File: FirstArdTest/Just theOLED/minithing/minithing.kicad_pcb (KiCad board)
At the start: 2 copper layers, 81.8 x 40.2 mm, 41 parts, among them IC1 DS3231MZ+, J1 USB4110-GF-A, Q1 NMOS, Q2 NMOS, Q3 FDN340P, SW1 SW_Push, SW2 SW_Push, SW3 SW_Push, SW4 SW_Push, U1 TP4056, U2 MT3608, U3 AHT20, U4 MCP23008-xSO

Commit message: Actual finish arduino pin change
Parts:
- SW3: footprint Button_Switch_THT:SW_PUSH_6mm_H4.3mm -> Button_Switch_THT:SW_PUSH_6mm
- U1: value TP4056 -> TP4056-42-ESOP8
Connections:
- A1 pad 19: unconnected-(A1-A0-Pad19) -> Net-(A1-A0)
- A1 pad 7: Net-(A1-D4) -> unconnected-(A1-D4-Pad7)
- C6 pad 2: Net-(A1-D4) -> Net-(A1-A0)
- R11 pad 1: Net-(A1-D4) -> Net-(A1-A0)
- R12 pad 1: Net-(A1-D4) -> Net-(A1-A0)
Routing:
- net Net-(A1-D4): track 52.5 -> 0.00 mm, vias 1 -> 0
- net (no net): track 0.00 -> 52.5 mm, vias 0 -> 1
- net Net-(A1-A0): track 0.00 -> 31.4 mm, vias 0 -> 1
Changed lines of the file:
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@@
 			(drillshape 0)
 			(scaleselection 1)
-			(outputdirectory "../")
+			(outputdirectory "../gbr files/")
 		)
 	)
@@
 	(net 13 "unconnected-(A1-D13-Pad16)")
 	(net 14 "5V out")
-	(net 15 "unconnected-(A1-A0-Pad19)")
+	(net 15 "Net-(A1-A0)")
 	(net 16 "unconnected-(A1-A3-Pad22)")
 	(net 17 "unconnected-(A1-~{RESET}-Pad28)")
@@
 	(net 25 "unconnected-(A1-D1{slash}TX-Pad1)")
 	(net 26 "unconnected-(A1-D8-Pad11)")
-	(net 27 "Net-(A1-D4)")
+	(net 27 "unconnected-(A1-D4-Pad7)")
 	(net 28 "1AMP")
 	(net 29 "Net-(D3-A)")
@@
 			(at 0 1.68 90)
 			(layer "F.Fab")
+			(hide yes)
 			(effects
 				(font
@@
 			(layers "F.Cu" "F.Mask" "F.Paste")
 			(roundrect_rratio 0.212766)
-			(net 27 "Net-(A1-D4)")
+			(net 15 "Net-(A1-A0)")
 			(pintype "passive")
 		)
@@
 			)
 		)
-		(property "Value" "TP4056"
+		(property "Value" "TP4056-42-ESOP8"
 			(at 0 3.4 0)
 			(layer "F.Fab")
@@
 			(layers "*.Cu" "*.Mask")
 			(remove_unused_layers no)
-			(net 27 "Net-(A1-D4)")
+			(net 27 "unconnected-(A1-D4-Pad7)")
 			(pinfunction "D4")
 			(pintype "bidirectional")
@@
 			(layers "*.Cu" "*.Mask")
 			(remove_unused_layers no)
-			(net 15 "unconnected-(A1-A0-Pad19)")
+			(net 15 "Net-(A1-A0)")
 			(pinfunction "A0")
 			(pintype "bidirectional")
@@
 			(layers "F.Cu" "F.Mask" "F.Paste")
 			(roundrect_rratio 0.208333)
-			(net 27 "Net-(A1-D4)")
+			(net 15 "Net-(A1-A0)")
 			(pintype "passive")
 		)
@@
 			(layers "F.Cu" "F.Mask" "F.Paste")
 			(roundrect_rratio 0.208333)
-			(net 27 "Net-(A1-D4)")
+			(net 15 "Net-(A1-A0)")
 			(pintype "passive")
 		)
@@
 		)
 	)
-	(footprint "Button_Switch_THT:SW_PUSH_6mm_H4.3mm"
+	(footprint "Button_Switch_THT:SW_PUSH_6mm"
 		(layer "F.Cu")
 		(at 47.3 63.5 90)
-		(descr "tactile push button, 6x6mm e.g. PHAP33xx series, height=4.3mm")
+		(descr "Generic 6mm SW tactile push button")
 		(tags "tact sw push 6mm")
 		(property "Reference" "SW3"
@@
 		)
 		(embedded_fonts no)
-		(model "${KICAD9_3DMODEL_DIR}/Button_Switch_THT.3dshapes/SW_PUSH_6mm_H4.3mm.step"
+		(model "${KICAD9_3DMODEL_DIR}/Button_Switch_THT.3dshapes/SW_PUSH_6mm.step"
 			(offset
 				(xyz 0 0 0)
@@
 	)
 	(segment
+		(start 71.75 35)
+		(end 71.75 36.75)
+		(width 0.2)
+		(layer "F.Cu")
+		(net 0)
+	)
+	(segment
+		(start 71.6 38.4)
+		(end 71.4 38.4)
+		(width 0.2)
+		(layer "F.Cu")
+		(net 0)
+	)
+	(segment
+		(start 71.75 36.75)
+		(end 71.75 38.25)
+		(width 0.2)
+		(layer "F.Cu")
+		(net 0)
+	)
+	(segment
+		(start 71.75 38.25)
+		(end 71.6 38.4)
+		(width 0.2)
+		(layer "F.Cu")
+		(net 0)
+	)
+	(segment
+		(start 71.4 38.4)
+		(end 71.3625 38.3625)
+		(width 0.2)
+		(layer "F.Cu")
+		(net 0)
+	)
+	(segment
+		(start 71.3625 38.3625)
+		(end 69.2 38.3625)
+		(width 0.2)
+		(layer "F.Cu")
+		(net 0)
+	)
+	(via
+		(at 71.75 36.75)
+		(size 0.6)
+		(drill 0.3)
+		(layers "F.Cu" "B.Cu")
+		(net 0)
+	)
+	(segment
+		(start 90.25 44)
+		(end 88.351 45.899)
+		(width 0.2)
+		(layer "B.Cu")
+		(net 0)
+	)
+	(segment
+		(start 76.75 41.75)
+		(end 89.75 41.75)
+		(width 0.2)
+		(layer "B.Cu")
+		(net 0)
+	)
+	(segment
+		(start 87.5 51)
+		(end 84 51)
+		(width 0.2)
+		(layer "B.Cu")
+		(net 0)
+	)
+	(segment
+		(start 88.351 45.899)
+		(end 88.351 50.149)
+		(width 0.2)
+		(layer "B.Cu")
+		(net 0)
+	)
+	(segment
+		(start 82 53)
+		(end 82 59)
+		(width 0.2)
+		(layer "B.Cu")
+		(net 0)
+	)
+	(segment
+		(start 82 59.25)
+		(end 82 59)
+		(width 0.2)
+		(layer "B.Cu")
+		(net 0)
+	)
+	(segment
+		(start 81.99 59.01)
+		(end 81.99 62.41)
+		(width 0.2)
+		(layer "B.Cu")
+		(net 0)
+	)
+	(segment
+		(start 84 51)
+		(end 82 53)
+		(width 0.2)
+		(layer "B.Cu")
+		(net 0)
+	)
+	(segment
+		(start 90.25 42.25)
+		(end 90.25 44)
+		(width 0.2)
+		(layer "B.Cu")
+		(net 0)
+	)
+	(segment
+		(start 89.75 41.75)
+		(end 90.25 42.25)
+		(width 0.2)
+		(layer "B.Cu")
+		(net 0)
+	)
+	(segment
+		(start 82 59)
+		(end 81.99 59.01)
+		(width 0.2)
+		(layer "B.Cu")
+		(net 0)
+	)
+	(segment
+		(start 88.351 50.149)
+		(end 87.5 51)
+		(width 0.2)
+		(layer "B.Cu")
+		(net 0)
+	)
+	(segment
+		(start 71.75 36.75)
+		(end 76.75 41.75)
+		(width 0.2)
+		(layer "B.Cu")
+		(net 0)
+	)
+	(segment
 		(start 57.9675 43.425001)
 		(end 57.492499 42.95)
@@
 	)
 	(segment
+		(start 70.46 36.72)
+		(end 69.3685 37.8115)
+		(width 0.5)
+		(layer "F.Cu")
+		(net 15)
+	)
+	(via
+		(at 70.46 36.72)
+		(size 0.6)
+		(drill 0.3)
+		(layers "F.Cu" "B.Cu")
+		(free yes)
+		(net 15)
+	)
+	(segment
+		(start 94.69 45.910768)
+		(end 84.778232 35.999)
+		(width 0.5)
+		(layer "B.Cu")
+		(net 15)
+	)
+	(segment
+		(start 94.69 47.17)
+		(end 94.69 45.910768)
+		(width 0.5)
+		(layer "B.Cu")
+		(net 15)
+	)
+	(segment
+		(start 84.778232 35.999)
+		(end 71.181 35.999)
+		(width 0.5)
+		(layer "B.Cu")
+		(net 15)
+	)
+	(segment
+		(start 71.181 35.999)
+		(end 70.46 36.72)
+		(width 0.5)
+		(layer "B.Cu")
+		(net 15)
+	)
+	(segment
 		(start 100.44 42.94)
 		(end 101 43.5)
@@
 	)
 	(segment
-		(start 71.75 35)
-		(end 71.75 36.75)
-		(width 0.2)
-		(layer "F.Cu")
-		(net 27)
-	)
-	(segment
-		(start 71.6 38.4)
-		(end 71.4 38.4)
-		(width 0.2)
-		(layer "F.Cu")
-		(net 27)
-	)
-	(segment
-		(start 71.75 36.75)
-		(end 71.75 38.25)
-		(width 0.2)
-		(layer "F.Cu")
-		(net 27)
-	)
-	(segment
-		(start 71.75 38.25)
-		(end 71.6 38.4)
-		(width 0.2)
-		(layer "F.Cu")
-		(net 27)
-	)
-	(segment
-		(start 71.4 38.4)
-		(end 71.3625 38.3625)
-		(width 0.2)
-		(layer "F.Cu")
-		(net 27)
-	)
-	(segment
-		(start 71.3625 38.3625)
-		(end 69.2 38.3625)
-		(width 0.2)
-		(layer "F.Cu")
-		(net 27)
-	)
-	(via
-		(at 71.75 36.75)
-		(size 0.6)
-		(drill 0.3)
-		(layers "F.Cu" "B.Cu")
-		(net 27)
-	)
-	(segment
-		(start 90.25 44)
-		(end 88.351 45.899)
-		(width 0.2)
-		(layer "B.Cu")
-		(net 27)
-	)
-	(segment
-		(start 76.75 41.75)
-		(end 89.75 41.75)
-		(width 0.2)
-		(layer "B.Cu")
-		(net 27)
-	)
-	(segment
-		(start 87.5 51)
-		(end 84 51)
-		(width 0.2)
-		(layer "B.Cu")
-		(net 27)
-	)
-	(segment
-		(start 88.351 45.899)
-		(end 88.351 50.149)
-		(width 0.2)
-		(layer "B.Cu")
-		(net 27)
-	)
-	(segment
-		(start 82 53)
-		(end 82 59)
-		(width 0.2)
-		(layer "B.Cu")
-		(net 27)
-	)
-	(segment
-		(start 82 59.25)
-		(end 82 59)
-		(width 0.2)
-		(layer "B.Cu")
-		(net 27)
-	)
-	(segment
-		(start 81.99 59.01)
-		(end 81.99 62.41)
-		(width 0.2)
-		(layer "B.Cu")
-		(net 27)
-	)
-	(segment
-		(start 84 51)
-		(end 82 53)
-		(width 0.2)
-		(layer "B.Cu")
-		(net 27)
-	)
-	(segment
-		(start 90.25 42.25)
-		(end 90.25 44)
-		(width 0.2)
-		(layer "B.Cu")
-		(net 27)
-	)
-	(segment
-		(start 89.75 41.75)
-		(end 90.25 42.25)
-		(width 0.2)
-		(layer "B.Cu")
-		(net 27)
-	)
-	(segment
-		(start 82 59)
-		(end 81.99 59.01)
-		(width 0.2)
-		(layer "B.Cu")
-		(net 27)
-	)
-	(segment
-		(start 88.351 50.149)
-		(end 87.5 51)
-		(width 0.2)
-		(layer "B.Cu")
-		(net 27)
-	)
-	(segment
-		(start 71.75 36.75)
-		(end 76.75 41.75)
-		(width 0.2)
-		(layer "B.Cu")
-		(net 27)
-	)
-	(segment

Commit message: Routine PCB ordered push, partial code
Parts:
- removed Z1: 1N4733A, SamacSys_Parts:DIOAD1405W86L465D235
- D2: footprint Diode_SMD:D_SMC_Handsoldering -> Diode_SMD:D_SMA
- moved C4 29.0 mm to (74.7, 27.4)
- moved D2 1.77 mm to (38.3, 34.3), turned to -90 degrees
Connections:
- A1 pad 27: 5V out -> 1AMP
- C4 pad 1: 1AMP -> Net-(Q3-D)
- C7 pad 1: 5V out -> 1AMP
- C8 pad 2: 5V out -> 1AMP
- D2 pad 1: GND -> 1AMP
- D2 pad 2: 1AMP -> GND
- D3 pad 1: 5V out -> 1AMP
- L1 pad 1: 1AMP -> Net-(Q3-D)
- Q3 pad 3: 1AMP -> Net-(Q3-D)
- R5 pad 2: 5V out -> 1AMP
- U2 pad 4: 1AMP -> Net-(Q3-D)
- U2 pad 5: 1AMP -> Net-(Q3-D)
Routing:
- net (no net): track 52.5 -> 0.00 mm, vias 1 -> 0
- net 1AMP: track 65.2 -> 87.5 mm, vias 2 -> 5
- net 5V out: track 19.3 -> 0.00 mm
- net Net-(Q3-D): track 0.00 -> 10.1 mm
- net Net-(A1-A0): track 31.4 -> 36.6 mm

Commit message: LastFinalFinalPush
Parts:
- added R13: 5.1KR, Resistor_SMD:R_0805_2012Metric_Pad1.20x1.40mm_HandSolder, F.Cu at (40.8, 50.3)
- added R14: 5.1KR, Resistor_SMD:R_0805_2012Metric_Pad1.20x1.40mm_HandSolder, F.Cu at (43.7, 50.3)
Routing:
- net Net-(A1-A4): track 55.6 -> 74.4 mm
- net Net-(A1-A5): track 60.3 -> 71.5 mm, vias 0 -> 2
- net Net-(A1-3V3): track 72.5 -> 81.5 mm

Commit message: DEADASS final finish last frealsies
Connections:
- IC1 pad 7: Net-(A1-A5) -> Net-(A1-A4)
- IC1 pad 8: Net-(A1-A4) -> Net-(A1-A5)
- R13 pad 2: Net-(A1-A4) -> Net-(A1-A5)
- R14 pad 2: Net-(A1-A5) -> Net-(A1-A4)
- U3 pad 3: Net-(A1-A4) -> Net-(A1-A5)
- U3 pad 4: Net-(A1-A5) -> Net-(A1-A4)
- U4 pad 1: Net-(A1-A4) -> Net-(A1-A5)
- U4 pad 2: Net-(A1-A5) -> Net-(A1-A4)
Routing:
- net Net-(A1-A4): track 74.4 -> 86.0 mm, vias 0 -> 3
- net Net-(A1-A5): track 71.5 -> 79.4 mm, vias 2 -> 0

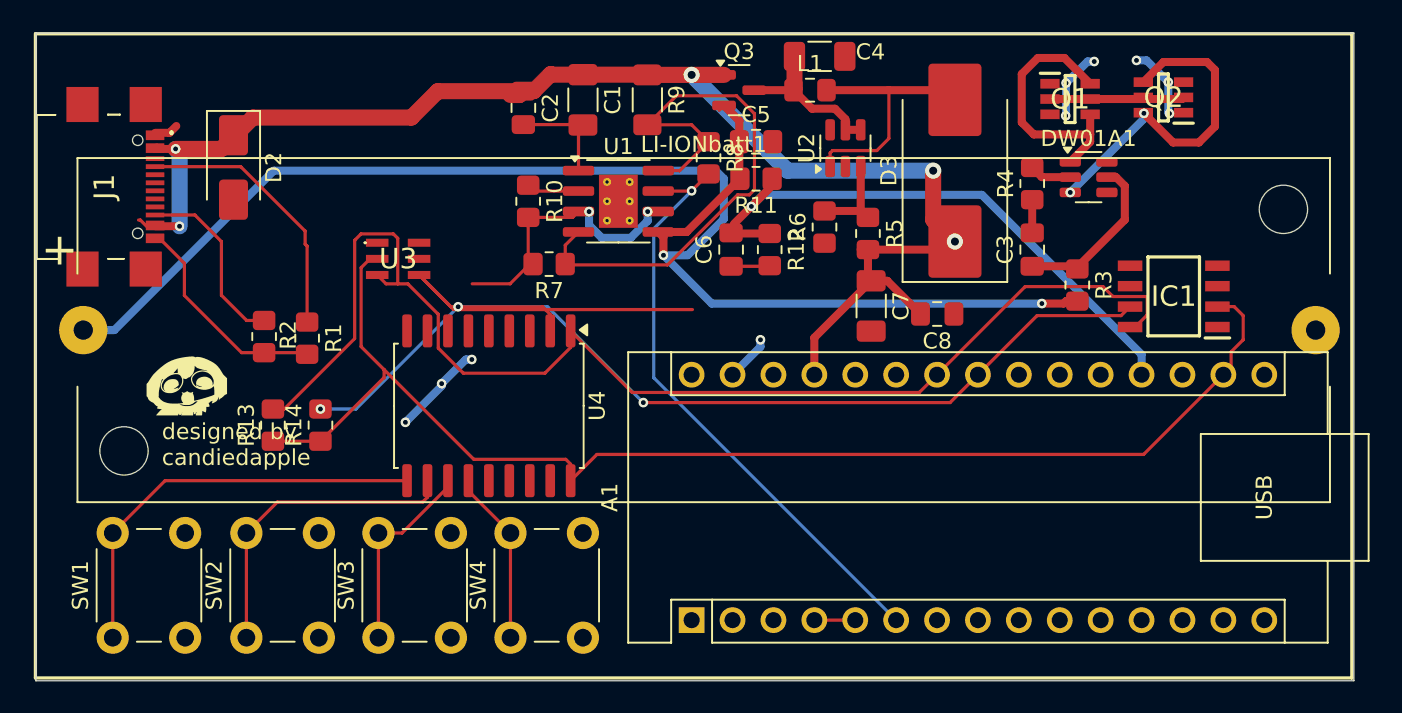
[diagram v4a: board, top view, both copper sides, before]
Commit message: Picture input push
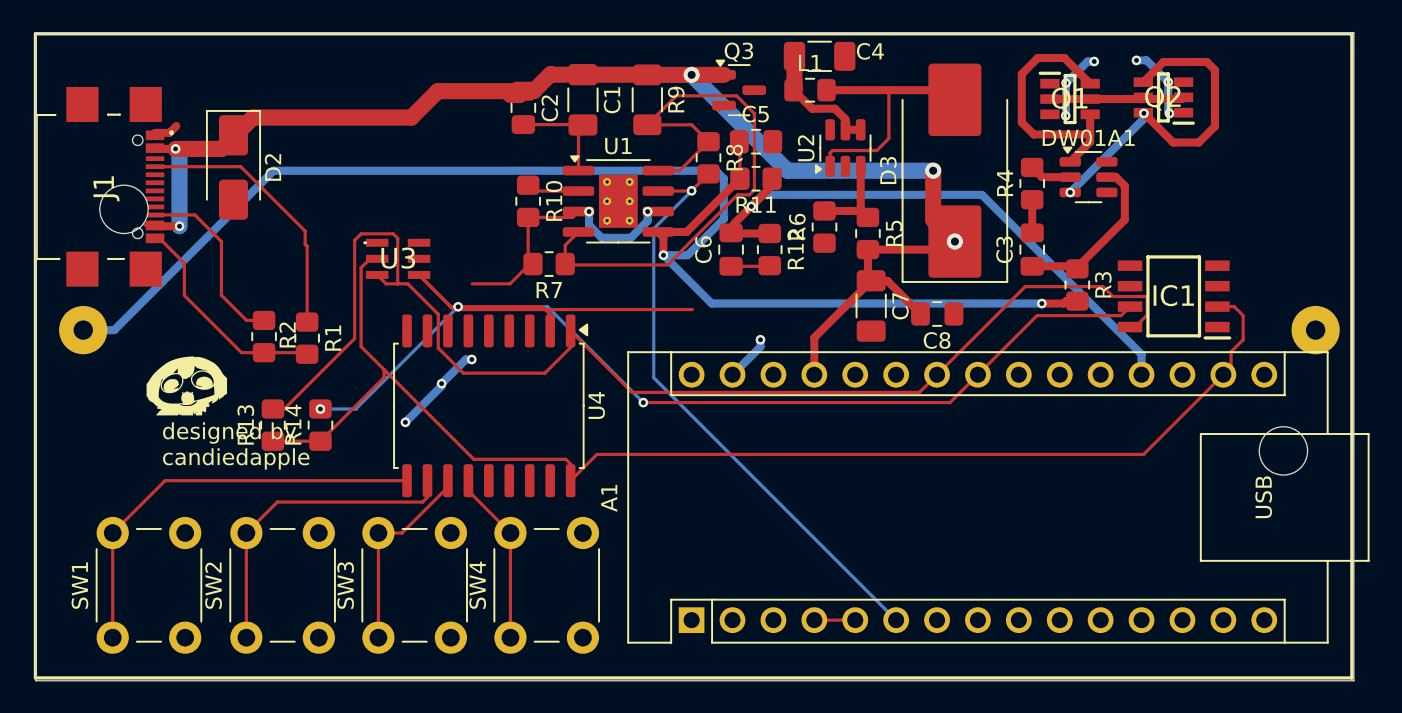
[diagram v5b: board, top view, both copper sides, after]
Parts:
- LI-IONbatt1: moved to B.Cu
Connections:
- C4 pad 1: Net-(Q3-D) -> Net-(Q3-S)
- L1 pad 1: Net-(Q3-D) -> Net-(Q3-S)
- Q3 pad 2: BATTERY -> Net-(Q3-S)
- Q3 pad 3: Net-(Q3-D) -> BATTERY
- U2 pad 4: Net-(Q3-D) -> Net-(Q3-S)
- U2 pad 5: Net-(Q3-D) -> Net-(Q3-S)
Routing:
- net Net-(Q3-D): track 10.1 -> 0.00 mm
- net Net-(Q3-S): track 0.00 -> 8.13 mm
- net BATTERY: track 100.9 -> 94.3 mm
